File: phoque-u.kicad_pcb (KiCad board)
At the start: 2 copper layers, 242.7 x 80.2 mm, 50 parts, among them J1 18…56 V, J2 On / Off, J3 3.3…24 V, Q1 SiR120DP, Q2 SiR120DP, Q3 SiR120DP, Q4 SiR120DP, SW1 Remote, SW2 Voltage select, T1 320 µ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

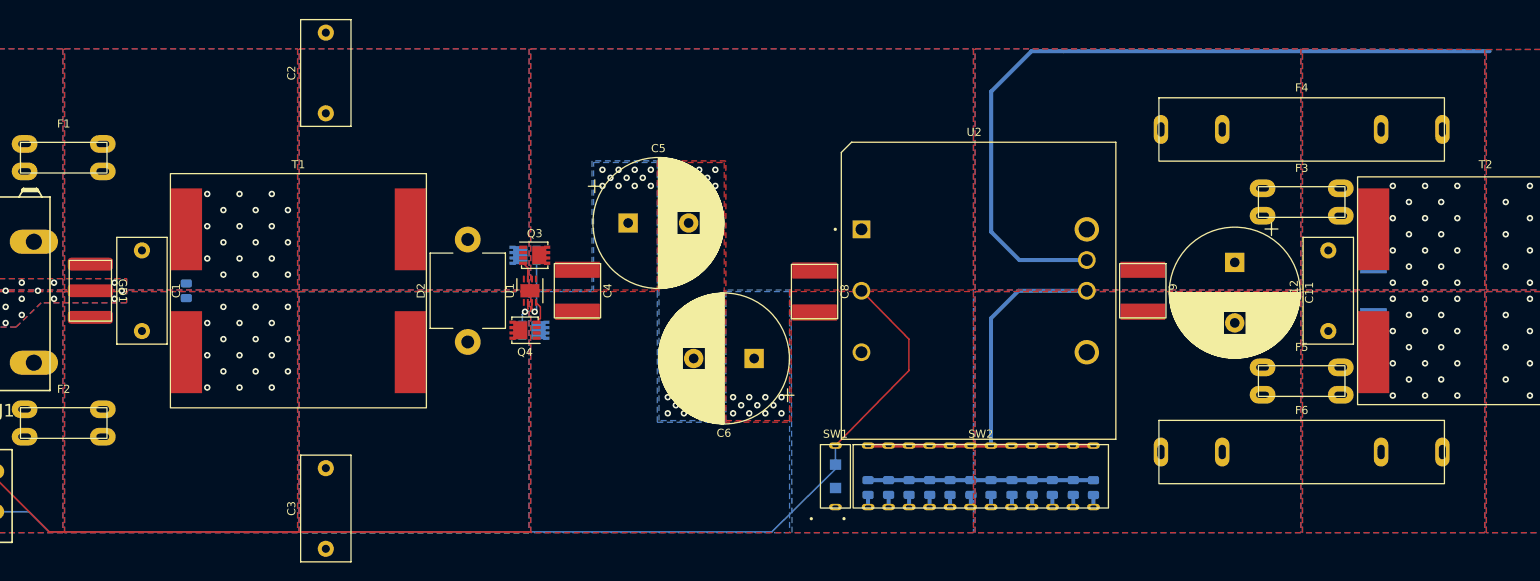
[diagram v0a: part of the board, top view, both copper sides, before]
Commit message: Optimise paths between rectifier and converter
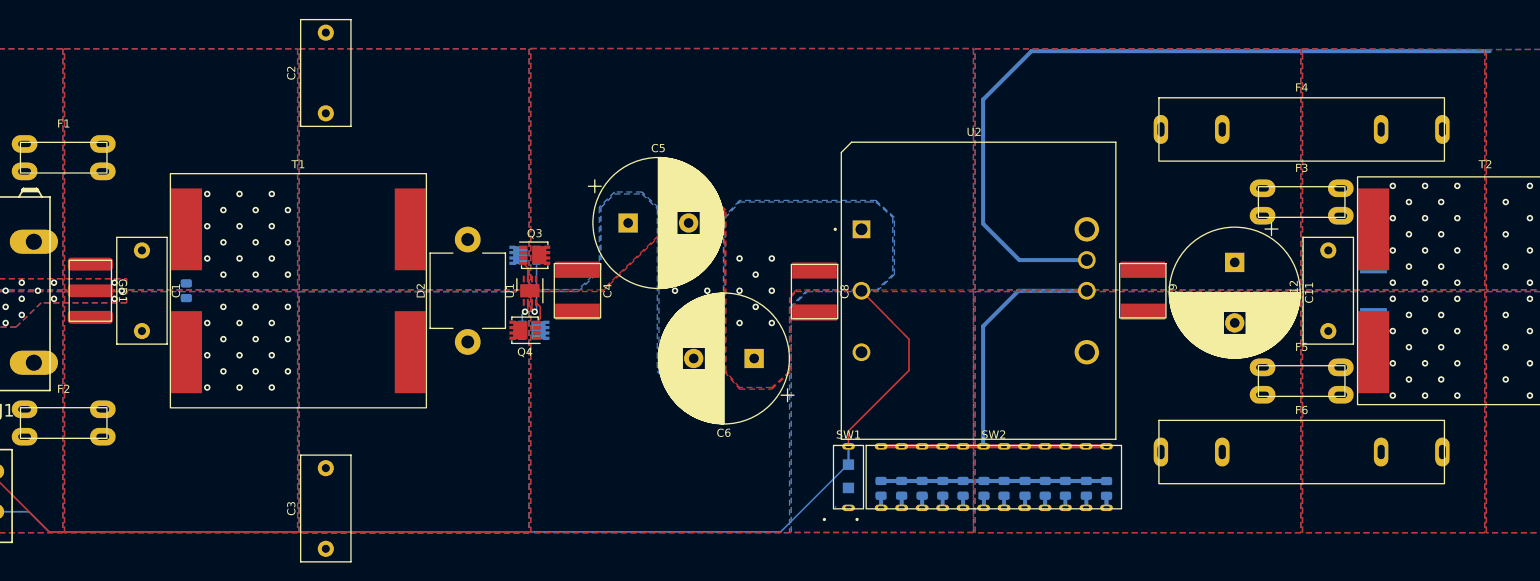
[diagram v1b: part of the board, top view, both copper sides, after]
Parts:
- moved R12 1.62 mm to (176.8, 123.0)
- moved R1 1.62 mm to (148.8, 123.0)
- moved R11 1.62 mm to (174.3, 123.0)
- moved R2 1.62 mm to (151.4, 123.0)
- moved R3 1.62 mm to (153.9, 123.0)
- moved R4 1.62 mm to (156.5, 123.0)
- moved R5 1.62 mm to (159.0, 123.0)
- moved R6 1.62 mm to (161.6, 123.0)
- moved R7 1.62 mm to (164.1, 123.0)
- moved SW1 1.62 mm to (144.8, 121.6)
- moved SW2 1.62 mm to (162.8, 121.6)
- moved R10 1.62 mm to (171.7, 123.0)
- moved R8 1.62 mm to (166.7, 123.0)
- moved R9 1.62 mm to (169.2, 123.0)
- moved D1 1.60 mm to (144.8, 121.5)
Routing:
- net /V_{outfilt}+: track 94.6 -> 95.4 mm
- net /On/Off: track 137.5 -> 138.1 mm
- net /Trim: track 57.0 -> 57.5 mm
- net /V_{in}-: vias 22 -> 8
- net /V_{in}+: vias 22 -> 8

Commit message: Add dedicated signal and ground layers
This reduces the board dimensions considerably.
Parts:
- Q1: moved to F.Cu
- Q4, U1: moved to B.Cu
- moved C13 32.2 mm to (206.8, 80.9), turned to 180 degrees
- moved C14 32.1 mm to (206.8, 116.1), turned to 0 degrees
- moved C6 31.0 mm to (103.9, 117.3), turned to 0 degrees
- moved C8 26.2 mm to (114.4, 98.5)
- moved C12 26.2 mm to (178.1, 98.5)
- moved C9 26.2 mm to (155.1, 98.5)
- moved R11 26.2 mm to (148.1, 123.0)
- moved R12 26.2 mm to (150.6, 123.0)
- moved R5 26.2 mm to (132.8, 123.0)
- moved SW2 26.2 mm to (136.6, 121.6)
- moved T2 26.2 mm to (197.6, 98.5)
- moved D1 26.2 mm to (118.6, 121.5), turned to 90 degrees
- moved R2 26.2 mm to (125.2, 123.0)
- moved SW1 26.2 mm to (118.6, 121.6)
- moved C11 26.2 mm to (166.5, 95.0)
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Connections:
- SW1 pad 1: /V_{in}- -> /On/Off
- SW1 pad 2: /On/Off -> /V_{in}-
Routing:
- net /V_{in}-: track 70.5 -> 114.4 mm, vias 8 -> 16
- net /V_{in}+: track 0.00 -> 20.5 mm, vias 8 -> 15
- net /G_{Q4}: track 2.88 -> 20.3 mm, vias 0 -> 2
- net /V_{outfilt}+: track 95.4 -> 80.3 mm, vias 14 -> 13
- net /On/Off: track 138.1 -> 123.9 mm
- net /G_{Q2}: track 7.40 -> 21.2 mm, vias 1 -> 2
- net /G_{Q3}: track 2.20 -> 14.4 mm, vias 0 -> 2
- net /G_{Q1}: track 2.74 -> 14.5 mm, vias 1 -> 2
- net /Trim: track 57.5 -> 52.6 mm
- net /V_{out}-: vias 0 -> 5
- net GND: vias 22 -> 28
- net /V_{out}+: vias 0 -> 5
- net /V_{outfuse}-: vias 18 -> 13
- net /V_{outfuse}+: vias 18 -> 13
- net /V_{outfilt}-: vias 14 -> 13
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- added copper zone on In2.Cu, net GND
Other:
- board size 242.7 x 80.2 mm -> 216.4 x 61 mm
- copper layers 2 -> 4

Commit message: Cut board to 212.3 × 75 cm
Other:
- board size 216.4 x 61 mm -> 212.3 x 75 mm
